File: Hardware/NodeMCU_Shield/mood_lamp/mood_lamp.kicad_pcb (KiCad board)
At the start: 2 copper layers, 27.1 x 59.1 mm, 8 parts, among them J1 Screw_Terminal_01x03, SW1 SW_Push, T1 BC548, U1 NodeMCU_Amica_R2

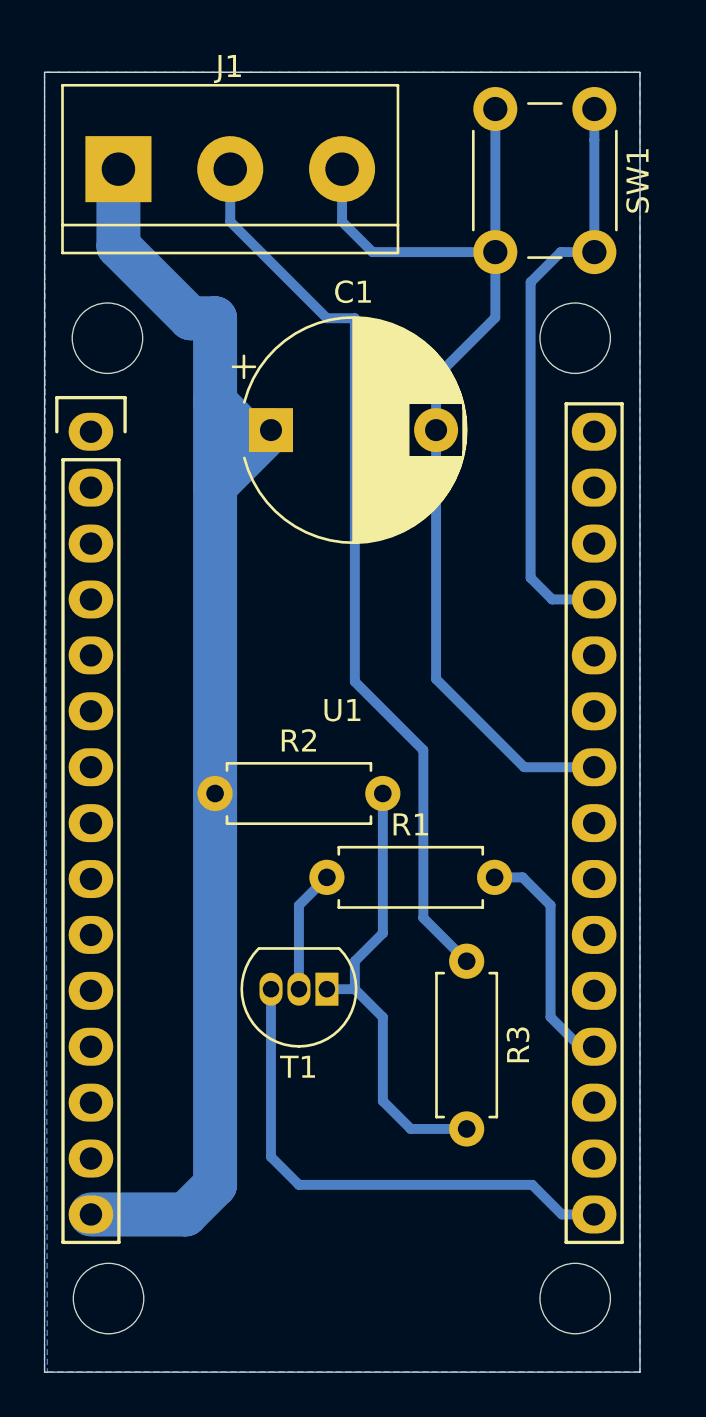
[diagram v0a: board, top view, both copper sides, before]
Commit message: Updated fritzing layouts. Fixed some issues with PCB design. Generated Gerber files.
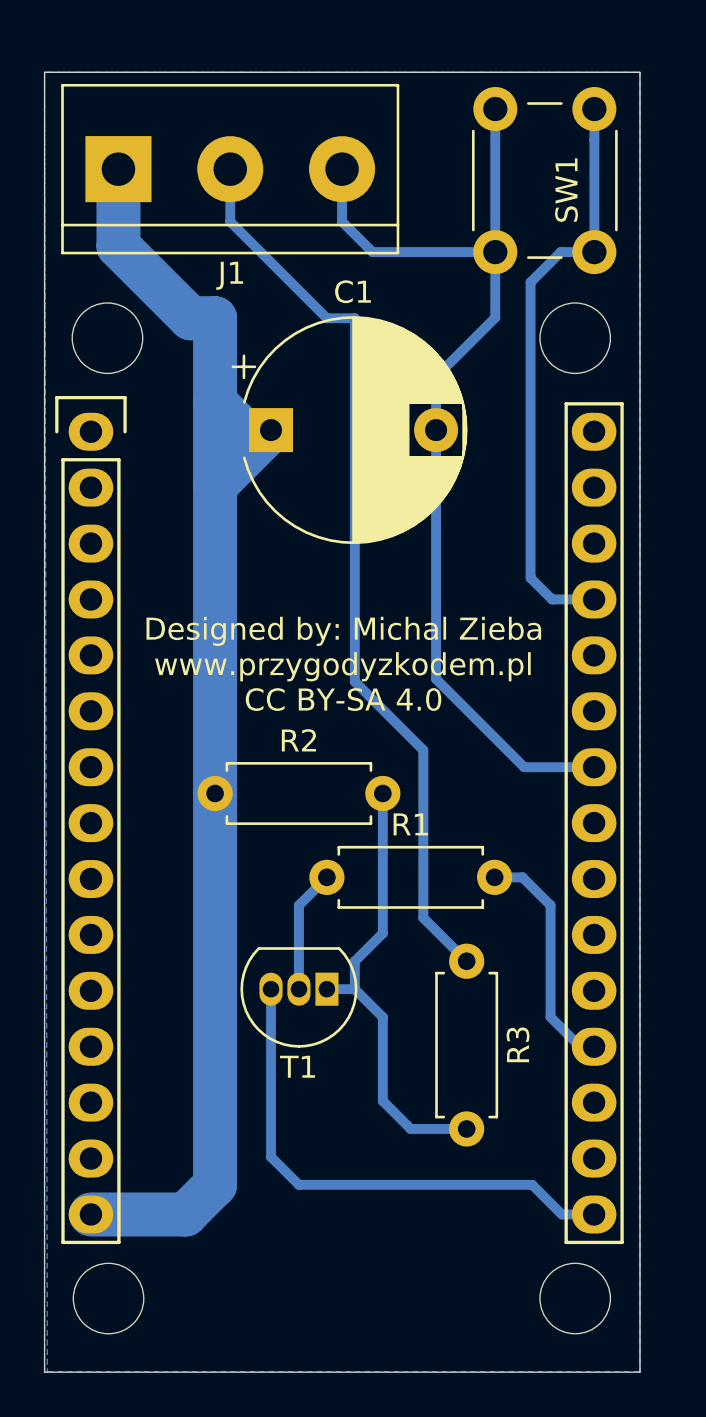
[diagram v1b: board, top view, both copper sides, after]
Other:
- board text added: "Designed by: Michal Zieba www.przygodyzkodem.pl CC BY-SA 4.0"
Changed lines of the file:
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@@
   (general
     (thickness 1.6)
-    (drawings 6)
+    (drawings 7)
     (tracks 60)
     (zones 0)
@@
     (pad_to_mask_clearance 0.051)
     (solder_mask_min_width 0.25)
-    (aux_axis_origin 0 0)
+    (aux_axis_origin 37.973 25.654)
+    (grid_origin 37.973 25.654)
     (visible_elements FFFFFF7F)
     (pcbplotparams
@@
       (viasonmask false)
       (mode 1)
-      (useauxorigin false)
+      (useauxorigin true)
       (hpglpennumber 1)
       (hpglpenspeed 20)
@@
       (plotinvisibletext false)
       (padsonsilk false)
-      (subtractmaskfromsilk false)
+      (subtractmaskfromsilk true)
       (outputformat 1)
       (mirror false)
-      (drillshape 1)
+      (drillshape 0)
       (scaleselection 1)
-      (outputdirectory ""))
+      (outputdirectory "gerber_files/"))
   )
   (net 0 "")
@@
     (descr "Through-hole-mounted NodeMCU 0.9")
     (tags nodemcu)
-    (fp_text reference U1 (at 11.43 12.68) (layer F.SilkS)
-      (effects (font (size 1 1) (thickness 0.15)))
-    )
-    (fp_text value NodeMCU_Amica_R2 (at 11.43 45.085) (layer F.Fab)
+    (fp_text reference U1 (at 11.43 12.68) (layer F.SilkS) hide
+      (effects (font (size 1 1) (thickness 0.15)))
+    )
+    (fp_text value NodeMCU_Amica_R2 (at 8.433999 22.022999) (layer F.Fab) hide
       (effects (font (size 2 2) (thickness 0.15)))
     )
@@
     (descr "simple 3-pin terminal block, pitch 5.08mm, revamped version of bornier3")
     (tags "terminal block bornier3")
-    (fp_text reference J1 (at 5.05 -4.65) (layer F.SilkS)
+    (fp_text reference J1 (at 5.153078 4.743299) (layer F.SilkS)
       (effects (font (size 1 1) (thickness 0.15)))
     )
@@
       (effects (font (size 1 1) (thickness 0.15)))
     )
-    (fp_text value 2.2k (at 3.81 2.37) (layer F.Fab)
+    (fp_text value 2.2k (at 3.048 2.286) (layer F.Fab)
       (effects (font (size 1 1) (thickness 0.15)))
     )
@@
       (effects (font (size 1 1) (thickness 0.15)))
     )
-    (fp_text value 6.8k (at 3.81 2.37) (layer F.Fab)
+    (fp_text value 6.8k (at 2.032 2.413) (layer F.Fab)
       (effects (font (size 1 1) (thickness 0.15)))
     )
@@
     (descr "tactile push button, 6x6mm e.g. PHAP33xx series, height=5mm")
     (tags "tact sw push 6mm")
-    (fp_text reference SW1 (at 3.25 -2 90) (layer F.SilkS)
+    (fp_text reference SW1 (at 3.665315 1.228876 90) (layer F.SilkS)
       (effects (font (size 1 1) (thickness 0.15)))
     )
@@
       (effects (font (size 1 1) (thickness 0.15)))
     )
-    (fp_text value BC548 (at 1.27 2.79) (layer F.Fab)
+    (fp_text value BC548 (at 1.397 -3.556) (layer F.Fab)
       (effects (font (size 1 1) (thickness 0.15)))
     )
@@
     )
   )
+  (gr_text "Designed by: Michal Zieba\nwww.przygodyzkodem.pl\nCC BY-SA 4.0" (at 51.562 52.578) (layer F.SilkS)
+    (effects (font (size 1 1) (thickness 0.25)))
+  )
   (gr_line (start 37.973 84.709) (end 38.1 84.709) (layer Edge.Cuts) (width 0.05))
